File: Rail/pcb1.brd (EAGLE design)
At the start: 49.7 x 86.4 mm, 45 parts, among them J6 638207222005, J7 638207222005, U4 TLE9250VSJ, X1 S4P-VH

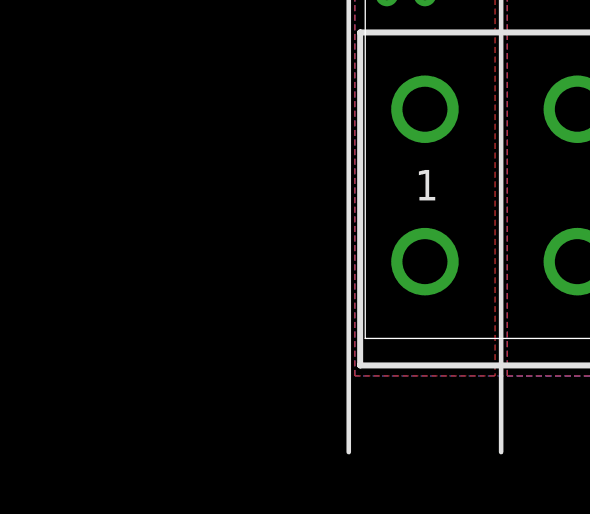
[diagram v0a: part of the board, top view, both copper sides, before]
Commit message: Cooling of LED !
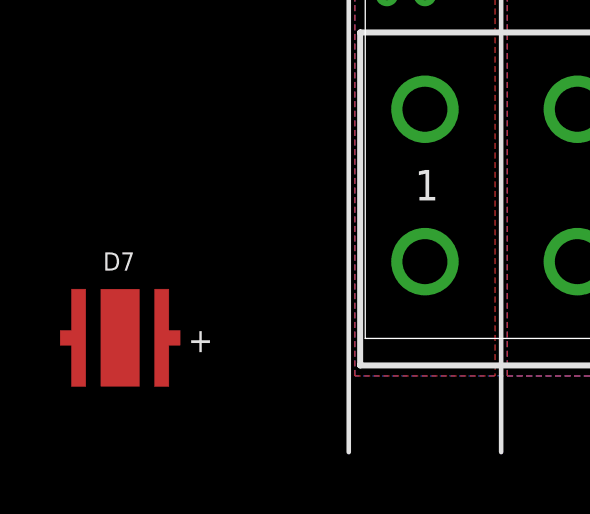
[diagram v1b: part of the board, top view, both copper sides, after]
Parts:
- added D7: 150353GS74500, LED:WL-SMDC_3535
- D1, D2, D3, D4: device Wurth_LEDs_WL-SMDC:WL-SMDC_3535 -> LED:WL-SMDC_3535
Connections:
- net Q1: now also D1.3
- net Q2: now also D2.3
- net Q3: now also D3.3
- net Q4: now also D4.3
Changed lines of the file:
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@@
 <attribute name="VCLAMP" value="53.3V" x="-20.066" y="-26.035" size="1.778" layer="27" display="off"/>
 </element>
-<element name="D2" library="Wurth_LEDs_WL-SMDC" library_urn="urn:adsk.eagle:library:19063442" package="WL-SMDC_3535" package3d_urn="urn:adsk.eagle:package:19063445/2" value="150353GS74500" x="-1.27" y="-25.4" smashed="yes" rot="R180">
+<element name="D2" library="LED" package="WL-SMDC_3535" package3d_urn="urn:adsk.eagle:package:19063445/2" value="150353GS74500" x="-1.27" y="-25.4" smashed="yes" rot="R180">
 <attribute name="CHIP-TECHNOLOGY" value="InGaN" x="-1.27" y="-25.4" size="1.778" layer="27" rot="R180" display="off"/>
 <attribute name="DATASHEET-URL" value="https://www.we-online.com/catalog/datasheet/150353GS74500.pdf" x="-1.27" y="-25.4" size="1.778" layer="27" rot="R180" display="off"/>
@@
 <attribute name="VIEWING-ANGLE" value="125°" x="-1.27" y="-25.4" size="1.778" layer="27" rot="R180" display="off"/>
 </element>
-<element name="D1" library="Wurth_LEDs_WL-SMDC" library_urn="urn:adsk.eagle:library:19063442" package="WL-SMDC_3535" package3d_urn="urn:adsk.eagle:package:19063445/2" value="150353GS74500" x="-8.89" y="-25.4" smashed="yes">
+<element name="D1" library="LED" package="WL-SMDC_3535" package3d_urn="urn:adsk.eagle:package:19063445/2" value="150353GS74500" x="-8.89" y="-25.4" smashed="yes">
 <attribute name="CHIP-TECHNOLOGY" value="InGaN" x="-8.89" y="-25.4" size="1.778" layer="27" display="off"/>
 <attribute name="DATASHEET-URL" value="https://www.we-online.com/catalog/datasheet/150353GS74500.pdf" x="-8.89" y="-25.4" size="1.778" layer="27" display="off"/>
@@
 <attribute name="VIEWING-ANGLE" value="125°" x="-8.89" y="-25.4" size="1.778" layer="27" display="off"/>
 </element>
-<element name="D4" library="Wurth_LEDs_WL-SMDC" library_urn="urn:adsk.eagle:library:19063442" package="WL-SMDC_3535" package3d_urn="urn:adsk.eagle:package:19063445/2" value="150353GS74500" x="19.05" y="-25.4" smashed="yes" rot="R180">
+<element name="D4" library="LED" package="WL-SMDC_3535" package3d_urn="urn:adsk.eagle:package:19063445/2" value="150353GS74500" x="19.05" y="-25.4" smashed="yes" rot="R180">
 <attribute name="CHIP-TECHNOLOGY" value="InGaN" x="27.94" y="-33.02" size="1.778" layer="27" rot="R180" display="off"/>
 <attribute name="DATASHEET-URL" value="https://www.we-online.com/catalog/datasheet/150353GS74500.pdf" x="27.94" y="-33.02" size="1.778" layer="27" rot="R180" display="off"/>
@@
 <attribute name="VIEWING-ANGLE" value="125°" x="27.94" y="-33.02" size="1.778" layer="27" rot="R180" display="off"/>
 </element>
-<element name="D3" library="Wurth_LEDs_WL-SMDC" library_urn="urn:adsk.eagle:library:19063442" package="WL-SMDC_3535" package3d_urn="urn:adsk.eagle:package:19063445/2" value="150353GS74500" x="11.43" y="-25.4" smashed="yes">
+<element name="D3" library="LED" package="WL-SMDC_3535" package3d_urn="urn:adsk.eagle:package:19063445/2" value="150353GS74500" x="11.43" y="-25.4" smashed="yes">
 <attribute name="CHIP-TECHNOLOGY" value="InGaN" x="-5.08" y="-10.16" size="1.778" layer="27" display="off"/>
 <attribute name="DATASHEET-URL" value="https://www.we-online.com/catalog/datasheet/150353GS74500.pdf" x="-5.08" y="-10.16" size="1.778" layer="27" display="off"/>
@@
 <attribute name="TYPE" value="Board Stacker" x="-10.414" y="0" size="1.778" layer="27" display="off"/>
 <attribute name="VALUE" x="-14.9116" y="-0.9442" size="0.8128" layer="27" align="bottom-right"/>
+</element>
+<element name="D7" library="LED" package="WL-SMDC_3535" package3d_urn="urn:adsk.eagle:package:19063445/2" value="150353GS74500" x="-33.02" y="-43.18" smashed="yes">
+<attribute name="CHIP-TECHNOLOGY" value="InGaN" x="-33.02" y="-43.18" size="1.778" layer="27" display="off"/>
+<attribute name="DATASHEET-URL" value="https://www.we-online.com/catalog/datasheet/150353GS74500.pdf" x="-33.02" y="-43.18" size="1.778" layer="27" display="off"/>
+<attribute name="EMITTING-COLOR" value="Green" x="-33.02" y="-43.18" size="1.778" layer="27" display="off"/>
+<attribute name="LAMDA-DOM-TYP" value="525nm" x="-33.02" y="-43.18" size="1.778" layer="27" display="off"/>
+<attribute name="LAMDA-PEAK-TYP" value="520nm" x="-33.02" y="-43.18" size="1.778" layer="27" display="off"/>
+<attribute name="NAME" x="-33.06" y="-40.94" size="0.6096" layer="25" align="bottom-center"/>
+<attribute name="PART-NUMBER" value="150353GS74500" x="-33.02" y="-43.18" size="1.778" layer="27" display="off"/>
+<attribute name="PHI-V-TYP" value="85lm" x="-33.02" y="-43.18" size="1.778" layer="27" display="off"/>
+<attribute name="V-F-TYP" value="3.4V" x="-33.02" y="-43.18" size="1.778" layer="27" display="off"/>
+<attribute name="VALUE" x="-33.29" y="-45.99" size="0.6096" layer="27" align="bottom-center"/>
+<attribute name="VIEWING-ANGLE" value="125°" x="-33.02" y="-43.18" size="1.778" layer="27" display="off"/>
 </element>
 </elements>
@@
 <contactref element="J7" pad="A4"/>
 <contactref element="D4" pad="2"/>
+<contactref element="D4" pad="3"/>
 </signal>
 <signal name="Q3">
@@
 <contactref element="J7" pad="3"/>
 <contactref element="D3" pad="2"/>
+<contactref element="D3" pad="3"/>
 </signal>
 <signal name="Q1C">
@@
 <vertex x="-4.8768" y="-44.45"/>
 </polygon>
+<contactref element="D2" pad="3"/>
 </signal>
 <signal name="Q1">
@@
 <vertex x="-5.2832" y="-44.45"/>
 </polygon>
+<contactref element="D1" pad="3"/>
 </signal>
 <signal name="AGNDU3">
@@
 <contactref element="D4" pad="1"/>
 <contactref element="R19" pad="1"/>
-<polygon width="0.1524" layer="1" isolate="0.254" thermals="no">
+<polygon width="0.1524" layer="1" isolate="0.254">
 <vertex x="20.32" y="-23.876"/>
 <vertex x="22.479" y="-23.876"/>
@@
 <contactref element="D2" pad="1"/>
 <contactref element="R20" pad="1"/>
-<polygon width="0.1524" layer="1" isolate="0.254" thermals="no">
+<polygon width="0.1524" layer="1" isolate="0.254">
 <vertex x="0" y="-23.876"/>
 <vertex x="2.159" y="-23.876"/>
@@
 <contactref element="D1" pad="1"/>
 <contactref element="R23" pad="2"/>
-<polygon width="0.1524" layer="1" isolate="0.254" thermals="no">
+<polygon width="0.1524" layer="1" isolate="0.254">
 <vertex x="-12.319" y="-23.876"/>
 <vertex x="-10.16" y="-23.876"/>
@@
 <contactref element="D3" pad="1"/>
 <contactref element="R24" pad="2"/>
-<polygon width="0.1524" layer="1" isolate="0.254" thermals="no">
+<polygon width="0.1524" layer="1" isolate="0.254">
 <vertex x="8.001" y="-23.876"/>
 <vertex x="10.16" y="-23.876"/>

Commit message: therm
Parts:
- removed D7: 150353GS74500, LED:WL-SMDC_3535
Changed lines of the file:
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@@
 <attribute name="VALUE" x="-14.9116" y="-0.9442" size="0.8128" layer="27" align="bottom-right"/>
-</element>
-<element name="D7" library="LED" package="WL-SMDC_3535" package3d_urn="urn:adsk.eagle:package:19063445/2" value="150353GS74500" x="-33.02" y="-43.18" smashed="yes">
-<attribute name="CHIP-TECHNOLOGY" value="InGaN" x="-33.02" y="-43.18" size="1.778" layer="27" display="off"/>
-<attribute name="DATASHEET-URL" value="https://www.we-online.com/catalog/datasheet/150353GS74500.pdf" x="-33.02" y="-43.18" size="1.778" layer="27" display="off"/>
-<attribute name="EMITTING-COLOR" value="Green" x="-33.02" y="-43.18" size="1.778" layer="27" display="off"/>
-<attribute name="LAMDA-DOM-TYP" value="525nm" x="-33.02" y="-43.18" size="1.778" layer="27" display="off"/>
-<attribute name="LAMDA-PEAK-TYP" value="520nm" x="-33.02" y="-43.18" size="1.778" layer="27" display="off"/>
-<attribute name="NAME" x="-33.06" y="-40.94" size="0.6096" layer="25" align="bottom-center"/>
-<attribute name="PART-NUMBER" value="150353GS74500" x="-33.02" y="-43.18" size="1.778" layer="27" display="off"/>
-<attribute name="PHI-V-TYP" value="85lm" x="-33.02" y="-43.18" size="1.778" layer="27" display="off"/>
-<attribute name="V-F-TYP" value="3.4V" x="-33.02" y="-43.18" size="1.778" layer="27" display="off"/>
-<attribute name="VALUE" x="-33.29" y="-45.99" size="0.6096" layer="27" align="bottom-center"/>
-<attribute name="VIEWING-ANGLE" value="125°" x="-33.02" y="-43.18" size="1.778" layer="27" display="off"/>
 </element>
 </elements>

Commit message: so far OK !
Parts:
- moved C6 5.85 mm to (-1.27, -9.53), turned to 90 degrees
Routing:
- net AGNDU3: track 19.4 -> 20.7 mm, vias 0 -> 2
- net Q4C: track 53.4 -> 54.6 mm
- net Q1C: track 47.5 -> 48.5 mm
- net AGNDU2: track 8.67 -> 9.49 mm, vias 0 -> 2

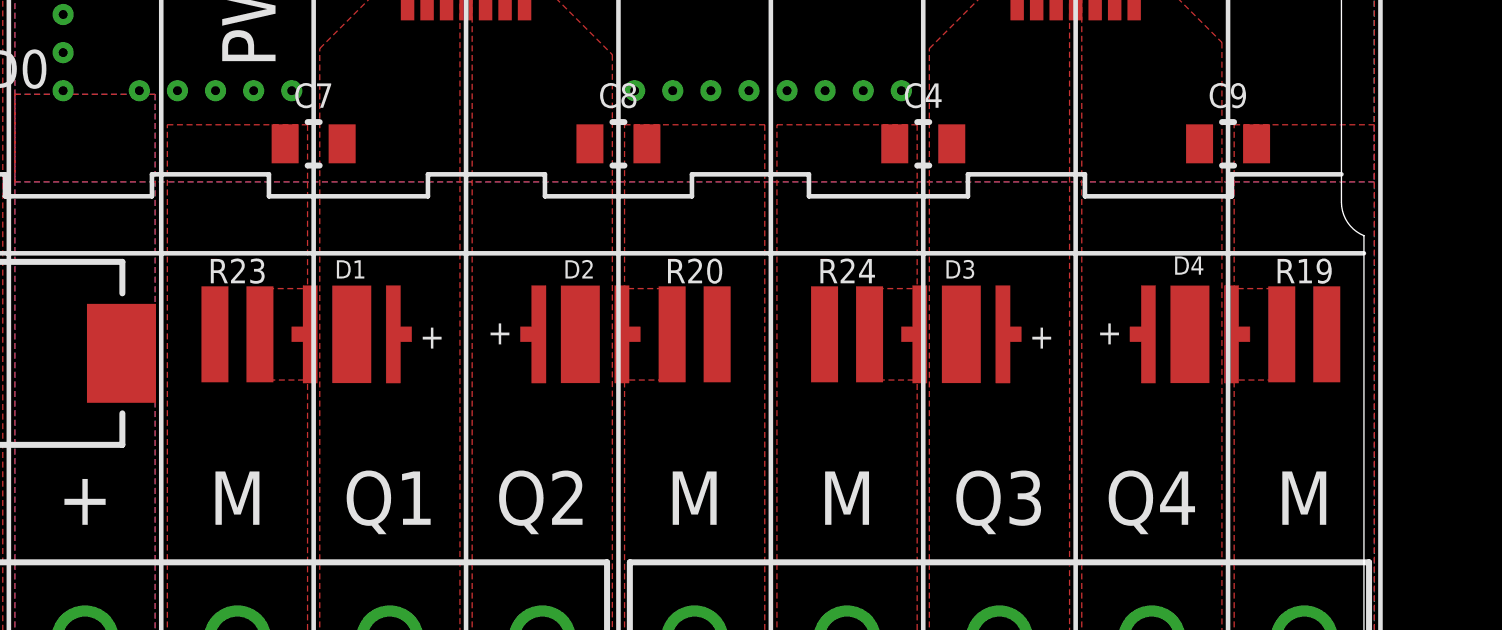
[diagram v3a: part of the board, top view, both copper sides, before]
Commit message: smaller LED
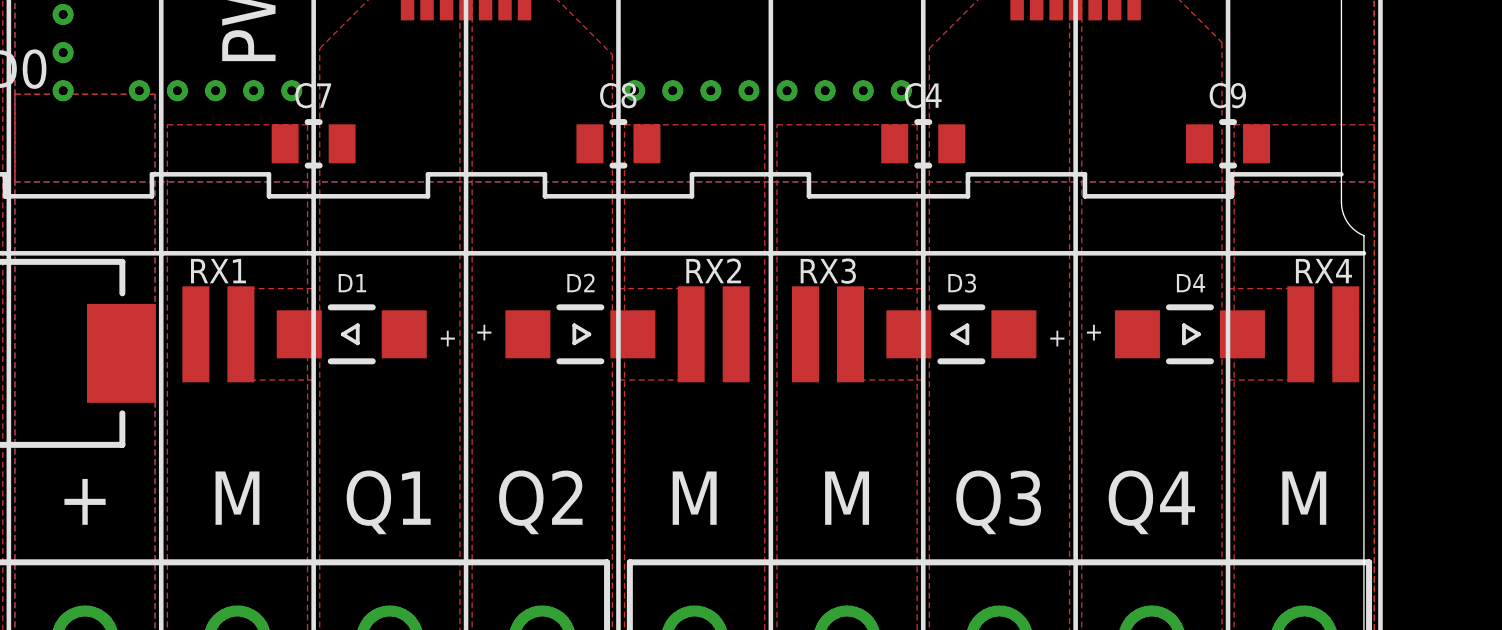
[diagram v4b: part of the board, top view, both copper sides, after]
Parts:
- removed R19, R20, R23, R24: 100Ohm, Wurth_Resistor_WRIS-KWKB:WRIS-KWKB_0612
- added RX1, RX2, RX3, RX4: 470Ohm, Wurth_Resistor_WRIS-KWKB:WRIS-KWKB_0612
- D1, D2, D3, D4: value 150353GS74500 -> (none); device LED:WL-SMDC_3535 -> Wurth_LEDs_WL-SMRW:WL-SMRW_1206_DOME
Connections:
- net N$1: now also RX4.1; no longer R19.1
- net N$6: now also RX2.1; no longer R20.1
- net N$8: now also RX1.2; no longer R23.2
- net N$9: now also RX3.2; no longer R24.2
- net PWR_GND: now also RX1.1, RX2.2, RX3.1, RX4.2; no longer R19.2, R20.2, R23.1, R24.1
- net Q1: no longer D1.3
- net Q2: no longer D2.3
- net Q3: no longer D3.3
- net Q4: no longer D4.3
